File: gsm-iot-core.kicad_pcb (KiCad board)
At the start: 2 copper layers, 38.1 x 61 mm, 95 parts, among them J1 MICRO_SD_HINGE - Micro SD soc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, P1 CONN_01X02, P2 CONN_01X04, P3 CONN_01X15, P4 CONN_01X17, P5 CONN_01X01, P6 CONN_01X01, P7 CONN_01X01, P8 CONN_01X01, P9 Chip anten, Q1 2SC1815, Q2 2SC1815, SW1 SW_PUSH, SW2 SW_PUSH, U1 STM32F405RGTx, U2 MP2365DN, U3 LP2985-50DBVR, U4 MMA7660, U5 SIM800C, U6 SIM HOLD - PPSS-6P, Y1 8MHz, Y2 32.768MHz

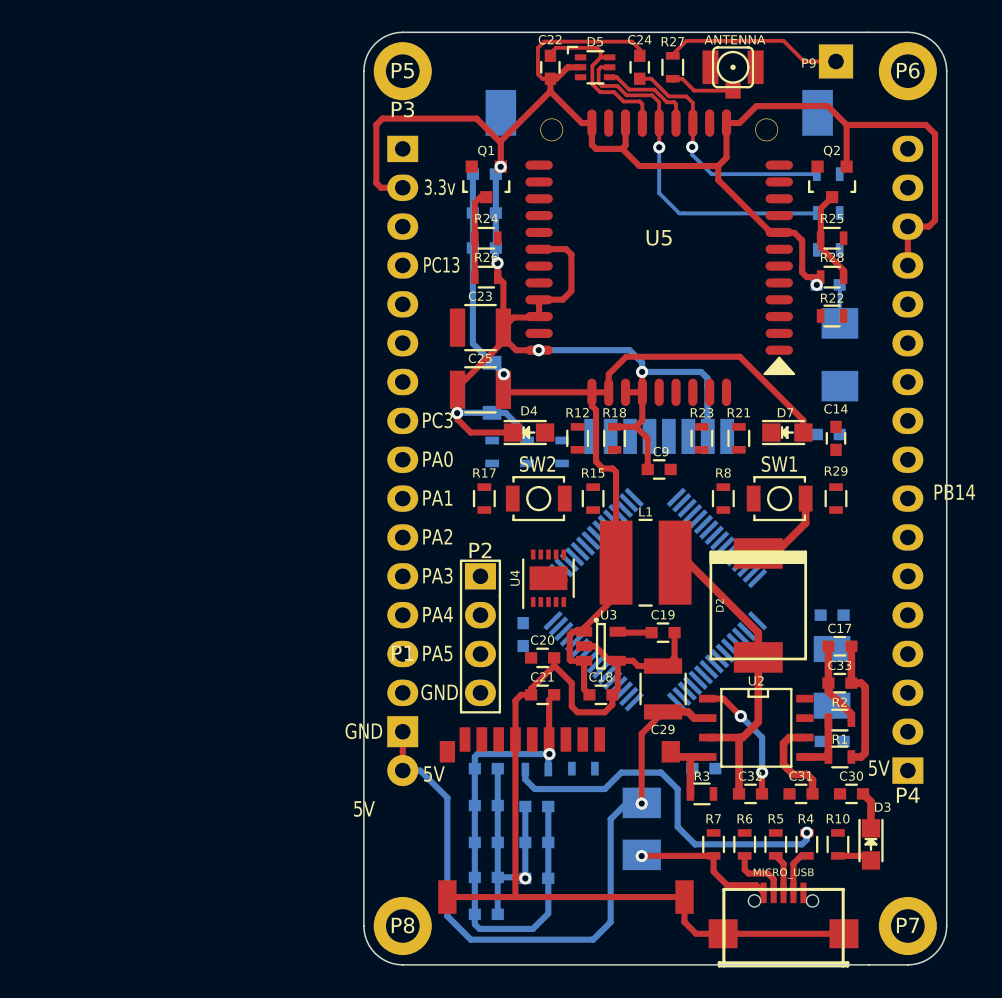
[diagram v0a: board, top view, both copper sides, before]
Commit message: Error add footprint-not updata footprint, local of component is bad
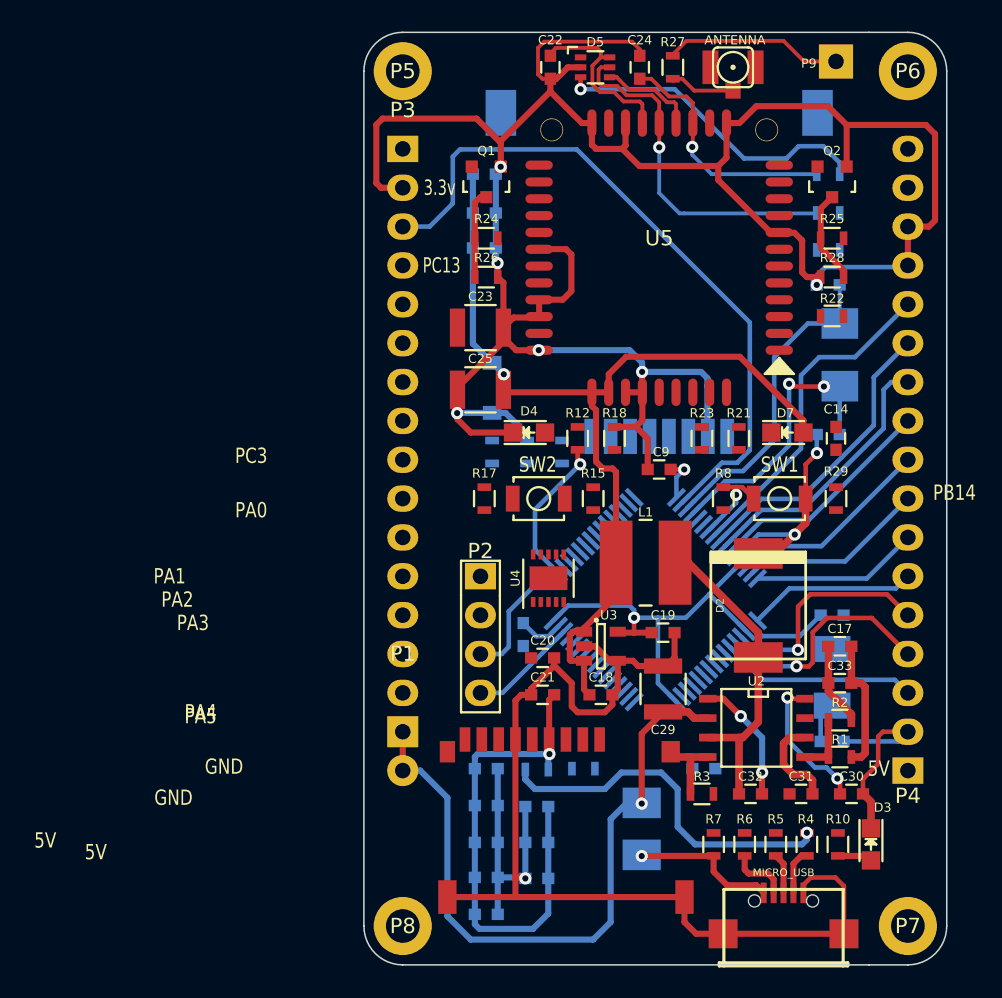
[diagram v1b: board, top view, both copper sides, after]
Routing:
- net PC13: track 0.00 -> 45.5 mm
- net GND: track 257.7 -> 296.4 mm, vias 7 -> 9
- net +3V3: track 35.5 -> 60.8 mm, vias 1 -> 2
- net PC0: track 0.00 -> 21.7 mm
- net Net-(D5-Pad3): track 0.00 -> 21.1 mm, vias 0 -> 1
- net PC1: track 0.00 -> 19.5 mm
- net Net-(C10-Pad1): track 0.00 -> 18.7 mm, vias 0 -> 2
- net Net-(C8-Pad1): track 2.53 -> 20.7 mm
- net PC2: track 0.00 -> 17.9 mm
- net PA5: track 0.00 -> 15.3 mm, vias 0 -> 1
- net PC3: track 0.00 -> 15.1 mm
- net PA4: track 0.00 -> 15.0 mm, vias 0 -> 1
- net PA0: track 0.00 -> 13.5 mm
- net PA6: track 0.00 -> 12.8 mm
- net PA1: track 0.00 -> 12.2 mm
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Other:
- net class Default: trace_width 0.25 -> 0.3
- rule trace_min: 0.25 -> 0.3

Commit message: add assets file and fix README
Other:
- board text removed: "GND"
- board text removed: "PA0"
- board text removed: "PA1"
- board text removed: "PA2"
- board text removed: "PA3"
- board text removed: "PA4"
- board text removed: "PA5"
- board text removed: "PC3"

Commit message: Fix error invalid foortprint- a error footprint file, add new footprint for component
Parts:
- removed ANT1: ANTENNA, w_conn_rf:coaxial_u.fl-r-smt-1
- removed C1, C16, C6: 4.7uF, Capacitors_SMD:C_0603
- removed C10, C8: 15pF, Capacitors_SMD:C_0603
- removed C11: 0.2uF, Capacitors_SMD:C_0603
- removed C12, C13: 27pF, Capacitors_SMD:C_0603
- removed C14, C2, C20, C21, C22, C3, C4, C5, C7, C9: 100nF, Capacitors_SMD:C_0603
- removed C15: 2.2uF, Capacitors_SMD:C_0603
- removed C17, C33: 22uF, Capacitors_SMD:C_0603
- removed C18, C19, C26: 10uF, Capacitors_SMD:C_0603
- removed C23, C25: 100uF, Capacitors_SMD:C_1210
- removed C24: 22pF, Capacitors_SMD:C_0603
- removed C27: 33pF, Capacitors_SMD:C_0603
- removed C28: 10pF, Capacitors_SMD:C_0603
- removed C29: 10uF/35V, Capacitors_SMD:C_1210
- removed C30: 0.1uF, Capacitors_SMD:C_0603
- removed C31: 4.7nF, Capacitors_SMD:C_0603
- removed C32: 10nF, Capacitors_SMD:C_0603
- removed CONN1: MICRO_USB, w_conn_pc:conn_usb_B_micro_smd-2
- removed D1: SS34, Diodes_SMD:DO-214BA
- removed D2: MBRS340, w_smd_diode:do214ab
- removed D3: Led_pwr, LEDs:LED_0805
- removed D4: PA15_LED, LEDs:LED_0805
- removed D5: SMF05C, TO_SOT_Packages_SMD:SC-70-6
- removed D6: zener 5.1v/500mW, Diodes_SMD:SOD-123
- removed D7: Led_SIM, LEDs:LED_0805
- removed J1: MICRO_SD_HINGE - Micro SD socket Push-Push A, lib:MicroSD_Push-Push-A
- removed L1: 6.8uH, Choke_SMD:Choke_SMD_Wuerth-WE-PD2-Typ-MS
- removed P1: CONN_01X02, Pin_Headers:Pin_Header_Straight_1x02
- removed P2: CONN_01X04, Pin_Headers:Pin_Header_Straight_1x04
- removed P3: CONN_01X15, Pin_Headers:Pin_Header_Straight_1x15
- removed P4: CONN_01X17, Pin_Headers:Pin_Header_Straight_1x17
- removed P5, P6, P7, P8: CONN_01X01, Mounting_Holes:MountingHole_2.2mm_M2_DIN965_Pad
- removed P9: Chip anten, Pin_Headers:Pin_Header_Straight_1x01
- removed Q1, Q2: 2SC1815, TO_SOT_Packages_SMD:SOT-23
- removed R1: 25.5k-1%, Resistors_SMD:R_0603
- removed R10, R16, R18, R8: 10k, Resistors_SMD:R_0603
- removed R11: 10M, Resistors_SMD:R_0603
- removed R12: 560R, Resistors_SMD:R_0603
- removed R13, R29, R9: 10K, Resistors_SMD:R_0603
- removed R14: 100k, Resistors_SMD:R_0603
- removed R15, R17, R25, R28: 4.7k, Resistors_SMD:R_0603
- removed R2: 7.5k-1%, Resistors_SMD:R_0603
- removed R21, R22, R23, R7: 1K, Resistors_SMD:R_0603
- removed R24, R26: 4k7, Resistors_SMD:R_0603
- removed R27: 0R, Resistors_SMD:R_0603
- removed R3: 20k, Resistors_SMD:R_0603
- removed R30, R31, R32, R5, R6: 22R, Resistors_SMD:R_0603
- removed R4: DNF-1K, Resistors_SMD:R_0603
- removed SW1, SW2: SW_PUSH, button:SW_SPST_B3U-1000P
- removed U1: STM32F405RGTx, lib:TQFP-64_10x10mm_Pitch0.5mm
- removed U2: MP2365DN, SMD_Packages:SOIC-8-N
- removed U3: LP2985-50DBVR, TO_SOT_Packages_SMD:SOT-23-5
- removed U4: MMA7660, Housings_DFN_QFN:DFN-10-1EP_3x3mm_Pitch0.5mm
- removed U5: SIM800C, lib:SIM800C
- removed U6: SIM HOLD - PPSS-6P, lib:SIM_HOLD_115A-ADA0-R02
- removed Y1: 8MHz, w_crystal:crystal_smd_5x3.2mm
- removed Y2: 32.768MHz, Crystals:Crystal_SMD_5032_2Pads
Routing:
- net GND: track 296.4 -> 0.00 mm, vias 9 -> 0
- net VDD: track 62.3 -> 0.00 mm, vias 1 -> 0
- net +3V3: track 60.8 -> 0.00 mm, vias 2 -> 0
- net PC13: track 45.5 -> 0.00 mm
- net +5V: track 44.6 -> 0.00 mm, vias 2 -> 0
- net PA10_ID: track 23.7 -> 0.00 mm, vias 1 -> 0
- net SIM800C_RST: track 22.9 -> 0.00 mm, vias 1 -> 0
- net PC0: track 21.7 -> 0.00 mm
- net Net-(D5-Pad3): track 21.1 -> 0.00 mm, vias 1 -> 0
- net Net-(C32-Pad1): track 20.8 -> 0.00 mm
- net Net-(C8-Pad1): track 20.7 -> 0.00 mm
- net PC1: track 19.5 -> 0.00 mm
- net Net-(C10-Pad1): track 18.7 -> 0.00 mm, vias 2 -> 0
- net PC2: track 17.9 -> 0.00 mm
- net SIM800C_DATA: track 16.2 -> 0.00 mm, vias 1 -> 0
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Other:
- board outline removed
- board text removed: "3.3v"
- board text removed: "5V"
- board text removed: "PB14"
- board text removed: "PC13"

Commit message: new PCB
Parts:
- added ANT1: ANTENNA, lib:coaxial_u.fl-r-smt-1, F.Cu at (291.8, 67.4)
- added C1: 4.7uF, Capacitors_SMD:C_0603, F.Cu at (151.8, 109.9)
- added C10: 15pF, lib:C_0603, F.Cu at (157.7, 92.6)
- added C11: 0.2uF, lib:C_0603, F.Cu at (157.7, 115.1)
- added C12: 10pF, lib:C_0603, F.Cu at (154.9, 92.7)
- added C13: 10pF, lib:C_0603, F.Cu at (149.1, 98.6)
- added C14: 100nF, lib:C_0603, F.Cu at (148.5, 89.2)
- added C15: 2.2uF, lib:C_0603, F.Cu at (169.2, 108.2)
- added C17: 0.1uF, lib:C_0603, F.Cu at (295.8, 72.1)
- added C18: 100nF, lib:C_0603, F.Cu at (157.7, 96.9)
- added C2: 100nF, Capacitors_SMD:C_0603, F.Cu at (159.9, 116.2)
- added C20: 4.7nF, lib:C_0603, F.Cu at (282.3, 85.2)
- added C21: 10nF, lib:C_0603, F.Cu at (315.1, 52.1)
- added C22: 22uF, lib:C_0603, F.Cu at (319.0, 48.7)
- added C23: 4.7uF, lib:C_0603, F.Cu at (324.3, 45.2)
- added C24: 22uF, lib:C_0603, F.Cu at (276.6, 94.0)
- added C25: 10uF, lib:C_0603, F.Cu at (315.1, 55.5)
- added C26: 10uF, lib:C_0603, F.Cu at (291.1, 76.4)
- added C27: 100nF, lib:C_0603, F.Cu at (291.1, 73.0)
- added C28: 100nF, lib:C_0603, F.Cu at (171.5, 89.2)
- added C29: 10uF/35V, Capacitors_SMD:C_1210, F.Cu at (307.2, 41.5)
- added C3: 100nF, Capacitors_SMD:C_0603, F.Cu at (170.3, 106.0)
- added C34: 100nF, lib:C_0603, F.Cu at (319.0, 52.1)
- added C35: 100nF, lib:C_0603, F.Cu at (165.2, 88.7)
- added C36: 22pF, lib:C_0603, F.Cu at (155.3, 88.7)
- added C37: 100uF, Capacitors_SMD:C_1210, F.Cu at (287.2, 67.7)
- added C38: 100uF, Capacitors_SMD:C_1210, F.Cu at (294.4, 61.1)
- added C39: 10uF, lib:C_0603, F.Cu at (304.7, 66.3)
- added C4: 100nF, Capacitors_SMD:C_0603, F.Cu at (160.3, 96.0)
- added C40: 33pF, lib:C_0603, F.Cu at (267.8, 95.4)
- added C41: 10pF, lib:C_0603, F.Cu at (300.8, 70.4)
- added C5: 100nF, Capacitors_SMD:C_0603, F.Cu at (150.9, 110.7)
- added C6: 4.7uF, Capacitors_SMD:C_0603, F.Cu at (150.0, 111.6)
- added C7: 100nF, Capacitors_SMD:C_0603, F.Cu at (149.1, 112.5)
- added C8: 15pF, lib:C_0603, F.Cu at (164.0, 92.6)
- added CONN1: MICRO_USB, lib:Micro_usb_B_smd, F.Cu at (149.9, 127.0)
- added D1: SS34, lib:do214ac, F.Cu at (114.6, 111.4)
- added D3: MBRS340, lib:do214ab, F.Cu at (287.4, 60.8)
- added D4: Led_pwr, LEDs:LED_0805, F.Cu at (278.5, 80.6)
- added D5: PA15_LED, LEDs:LED_0805, F.Cu at (300.9, 49.6)
- added D6: SMF05C, TO_SOT_Packages_SMD:SC-70-6, F.Cu at (171.5, 85.3)
- added D7: zener 5.1v/500mW, Diodes_SMD:SOD-123, F.Cu at (275.6, 60.4)
- added D8: Led_SIM, LEDs:LED_0805, F.Cu at (300.2, 55.0)
- added J1: MICRO_SD_HINGE - Micro SD socket Push-Push A, MicroSD_Push-Push-A, F.Cu at (171.4, 114.3)
- added L1: 3.3uH-3.2A, Choke_SMD:Choke_SMD_Wuerth-WE-PD2-Typ-MS, F.Cu at (272.8, 69.4)
- added P1: CONN_01X02, Pin_Headers:Pin_Header_Straight_1x02, F.Cu at (182.9, 119.4)
- added P2: CONN_01X04, Pin_Headers:Pin_Header_Straight_1x04, F.Cu at (174.0, 99.1)
- added P3: CONN_01X15, Pin_Headers:Pin_Header_Straight_1x15, F.Cu at (182.9, 78.7)
- added P4: CONN_01X17, Pin_Headers:Pin_Header_Straight_1x17, F.Cu at (137.2, 119.4)
- added P5: Chip anten, lib:point_test, F.Cu at (245.1, 71.1)
- added Q1: 2SC1815, lib:SOT-23, F.Cu at (308.2, 46.9)
- added Q2: 2SC1815, lib:SOT-23, F.Cu at (266.1, 89.0)
- added R10: 20k, lib:R_0603, F.Cu at (284.0, 88.1)
- added R11: 7.5k-1%, lib:R_0603, F.Cu at (263.5, 94.8)
- added R12: 25.5k-1%, lib:R_0603, F.Cu at (270.7, 76.5)
- added R13: 10k, lib:R_0603, F.Cu at (318.5, 54.9)
- added R14: 10M, lib:R_0603, F.Cu at (304.2, 69.1)
- added R15: 560R, lib:R_0603, F.Cu at (298.3, 74.9)
- added R16: 10K, lib:R_0603, F.Cu at (171.5, 87.8)
- added R17: 100k, lib:R_0603, F.Cu at (170.1, 109.1)
- added R18: 4.7k, lib:R_0603, F.Cu at (168.2, 92.6)
- added R19: 10k, lib:R_0603, F.Cu at (171.5, 93.8)
- added R20: 4.7k, lib:R_0603, F.Cu at (166.8, 92.6)
- added R21: 10k, lib:R_0603, F.Cu at (153.3, 114.0)
- added R22: 22R, lib:R_0603, F.Cu at (163.1, 89.7)
- added R23: 22R, lib:R_0603, F.Cu at (160.2, 89.7)
- added R24: 22R, lib:R_0603, F.Cu at (157.3, 89.7)
- added R25: 1K, lib:R_0603, F.Cu at (308.0, 70.1)
- added R26: 1K, lib:R_0603, F.Cu at (299.1, 78.5)
- added R27: 1K, lib:R_0603, F.Cu at (287.8, 89.9)
- added R28: 4k7, lib:R_0603, F.Cu at (295.3, 82.0)
- added R29: 0R, lib:R_0603, F.Cu at (322.2, 55.1)
- added R30: 4.7k, lib:R_0603, F.Cu at (304.2, 72.7)
- added R31: 4k7, lib:R_0603, F.Cu at (316.5, 58.5)
- added R32: 4.7k, lib:R_0603, F.Cu at (287.8, 86.3)
- added R33: 10K, lib:R_0603, F.Cu at (284.0, 91.6)
- added R4: DNF-1K, lib:R_0603, F.Cu at (152.0, 120.7)
- added R5: 22R, lib:R_0603, F.Cu at (150.6, 120.7)
- added R6: 22R, lib:R_0603, F.Cu at (149.1, 120.7)
- added R7: 1K, lib:R_0603, F.Cu at (147.7, 120.7)
- added R8: 10k, lib:R_0603, F.Cu at (148.5, 87.8)
- added R9: 10K, lib:R_0603, F.Cu at (165.4, 92.6)
- added SW1: SW_PUSH, lib:SW_SPST_B3U-1000P-B, F.Cu at (148.5, 91.5)
- added SW3: SW_PUSH, lib:SW_SPST_B3U-1000P-B, F.Cu at (171.5, 91.5)
- added U1: MP2365DN, SMD_Packages:SOIC-8-N, F.Cu at (117.0, 113.2)
- added U2: LP2985-50DBVR, TO_SOT_Packages_SMD:SOT-23-5, F.Cu at (260.6, 83.0)
- added U3: STM32F405RGTx, lib:TQFP-64_10x10mm_Pitch0.5mm, F.Cu at (160.0, 105.9)
- added U4: MMA7660, Housings_DFN_QFN:DFN-10-1EP_3x3mm_Pitch0.5mm, F.Cu at (190.2, 95.5)
- added U5: SIM800C, lib:SIM800C, F.Cu at (160.2, 76.4)
- added U6: SIM HOLD - PPSS-6P, SIM_HOLD_115A-ADA0-R02, B.Cu at (160.0, 87.6)
- added X1: CRYSTAL-24M, lib:Crystal_SMD_5032_4Pads, F.Cu at (152.0, 95.6)
- added Y3: 32.768MHz, lib:crystal_smd_32.768_2Pin, F.Cu at (160.8, 92.6)
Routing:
- net GND: track 0.00 -> 15.3 mm
- net Net-(C8-Pad1): track 0.00 -> 14.1 mm
- net Net-(C12-Pad2): track 0.00 -> 11.6 mm
- net Net-(C10-Pad1): track 0.00 -> 10.7 mm
- net Net-(C13-Pad1): track 0.00 -> 8.79 mm
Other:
- board outline added: 51.2 x 68.6 mm

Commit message: fix 3th
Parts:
- C17, C20, C21, C22, C24, C25, C26, C27, C29, C34, C35, C36, D3, L1, R10, R11, R12, R21, R22, R23, R24, U1, U2, U4: moved to B.Cu
- moved C21 183.1 mm to (148.0, 126.9)
- moved R13 182.8 mm to (148.1, 121.0), turned to 270 degrees
- moved C29 179.4 mm to (148.0, 124.1), turned to 90 degrees
- moved C22 174.6 mm to (162.3, 125.7), turned to 180 degrees
- moved C23 173.8 mm to (158.3, 96.5), turned to 225 degrees
- moved C25 161.9 mm to (168.5, 124.5), turned to 270 degrees
- moved R30 161.5 mm to (142.7, 75.1)
- moved R31 161.3 mm to (155.3, 64.8), turned to 270 degrees
- moved D5 160.5 mm to (157.1, 121.0), turned to 90 degrees
- moved C34 160.0 mm to (172.2, 115.6)
- moved R25 158.7 mm to (149.4, 75.5)
- moved Q1 157.7 mm to (151.5, 64.6), turned to 180 degrees
- moved D3 152.6 mm to (146.3, 118.7), turned to 180 degrees
- moved D8 151.5 mm to (149.0, 64.8), turned to 270 degrees
- moved R26 149.7 mm to (149.4, 76.9)
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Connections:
- P3 pad 10: PB12 -> PC13
- P3 pad 11: PB11 -> PB9
- P3 pad 12: PB10 -> PB8
- P3 pad 13: PB1 -> PB4
- P3 pad 2: GND -> +3V3
- P3 pad 3: PC13 -> GND
- P3 pad 4: PB9 -> PA1
- P3 pad 5: PB8 -> PA0
- P3 pad 6: PB4 -> PC3
- P3 pad 7: PB15 -> PC2
- P3 pad 8: PB14 -> PC1
- P3 pad 9: PB13 -> PC0
- P4 pad 1: +3V3 -> VBAT
- P4 pad 10: PC3 -> PB1
- P4 pad 11: PC2 -> PA6
- P4 pad 12: PC1 -> PA5
- P4 pad 13: PC0 -> PA4
- P4 pad 14: GND -> PA3
- P4 pad 15: GND -> PA2
- P4 pad 16: +3V3 -> GND
- P4 pad 17: VBAT -> +3V3
- P4 pad 2: GND -> +3V3
- P4 pad 3: PA6 -> GND
- P4 pad 4: PA5 -> PB15
- P4 pad 5: PA4 -> PB14
- P4 pad 6: PA3 -> PB13
- P4 pad 7: PA2 -> PB12
- P4 pad 8: PA1 -> PB11
- P4 pad 9: PA0 -> PB10
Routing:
- net GND: track 15.3 -> 81.5 mm, vias 0 -> 1
- net SIM800C_RST: track 0.00 -> 28.3 mm, vias 0 -> 1
- net PA4: track 0.00 -> 23.9 mm
- net PA5: track 0.00 -> 22.2 mm
- net SIM800C_CLK: track 0.00 -> 21.5 mm, vias 0 -> 1
- net PA6: track 0.00 -> 20.9 mm
- net PB15: track 0.00 -> 20.5 mm
- net +3V3: track 0.00 -> 20.5 mm, vias 0 -> 1
- net PB4: track 0.00 -> 19.6 mm, vias 0 -> 1
- net PB1: track 0.00 -> 18.9 mm
- net PB14: track 0.00 -> 18.2 mm
- net PB10: track 0.00 -> 17.4 mm
- net PB13: track 0.00 -> 17.1 mm
- net PC13: track 0.00 -> 17.1 mm, vias 0 -> 1
- net PB9: track 0.00 -> 17.1 mm, vias 0 -> 1
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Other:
- board size 51.2 x 68.6 mm -> 44.7 x 67.6 mm
- net class Default: via_dia 0.8 -> 1.1; via_drill 0.4 -> 0.6

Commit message: PCB new
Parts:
- added D4 (x3): Led_pwr, LEDs:LED_0805, F.Cu at (149.6, 121.0)
- added P8: CONN_01X01, lib:MountingHole_2.5mm, F.Cu at (140.3, 122.6)
- added P8: CONN_01X01, lib:MountingHole_2.5mm, F.Cu at (140.3, 69.2)
- added P8: CONN_01X01, lib:MountingHole_2.5mm, F.Cu at (179.7, 69.2)
- added P8: CONN_01X01, lib:MountingHole_2.5mm, F.Cu at (179.7, 122.6)
- D6: moved to B.Cu
- U3: footprint lib:TQFP-64_10x10mm_Pitch0.5mm -> TQFP-64_10x10mm_Pitch0.5mm
- moved R30 30.5 mm to (172.7, 80.5), turned to 180 degrees
- moved R32 30.0 mm to (172.7, 73.9)
- moved P5 28.6 mm to (148.3, 68.8)
- moved ANT1 23.7 mm to (151.3, 64.4)
- moved R29 23.7 mm to (151.3, 68.0)
- moved Q2 18.0 mm to (172.4, 77.2), turned to 270 degrees
- moved R28 18.0 mm to (148.0, 80.5), turned to 0 degrees
- moved R27 17.2 mm to (158.6, 88.6), turned to 90 degrees
- moved R25 16.9 mm to (160.0, 88.6), turned to 90 degrees
- moved R26 16.8 mm to (161.4, 88.6), turned to 90 degrees
- moved C37 15.0 mm to (160.0, 64.4)
- moved L1 14.5 mm to (146.7, 118.7), turned to 270 degrees
- moved C34 13.9 mm to (166.1, 128.2)
- moved Q1 13.0 mm to (147.6, 77.1), turned to 90 degrees
- moved R31 11.7 mm to (148.0, 73.9), turned to 0 degrees
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- renumbered SW1 to RST
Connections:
- P1 pad 2: +5V -> VBAT
- P4 pad 1: VBAT -> +3V3
- P4 pad 2: +3V3 -> GND
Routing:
- net GND: track 81.5 -> 409.3 mm, vias 1 -> 17
- net +3V3: track 20.5 -> 252.0 mm, vias 1 -> 15
- net VDD: track 11.0 -> 117.7 mm, vias 0 -> 5
- net SIM800C_DATA: track 9.05 -> 65.4 mm, vias 1 -> 4
- net /PB2: track 0.00 -> 54.5 mm, vias 0 -> 5
- net PA7_PWRKEY: track 0.00 -> 45.6 mm, vias 0 -> 4
- net +5V: track 5.75 -> 42.2 mm, vias 1 -> 2
- net SIM800C_TXD: track 0.00 -> 33.5 mm, vias 0 -> 2
- net PB3_BUTTON: track 0.00 -> 32.2 mm, vias 0 -> 2
- net PA2: track 0.00 -> 31.5 mm, vias 0 -> 3
- net SIM800C_RXD: track 0.00 -> 31.5 mm, vias 0 -> 2
- net PA3: track 0.00 -> 29.3 mm, vias 0 -> 3
- net /PB5: track 6.93 -> 36.1 mm, vias 0 -> 1
- net /RST: track 0.00 -> 27.7 mm, vias 0 -> 2
- net PC3: track 0.00 -> 26.8 mm, vias 0 -> 1
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- added copper zone on B.Cu, net GND
- added copper zone on F.Cu, net GND
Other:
- board text added: "3.3V"
- board text added: "5V"
- board text added: "GND"
- board text added: "PA0"
- board text added: "PA1"
- board text added: "PA2"
- board text added: "PA3"
- board text added: "PA4"
- board text added: "PA5"
- board text added: "PA6"
- board text added: "PB1"
- board text added: "PB10"
- board text added: "PB11"
- board text added: "PB12"
- board text added: "PB13"
- board text added: "PB14"
- board text added: "PB15"
- board text added: "PC0"
- board text added: "PC1"
- board text added: "PC13"
- board text added: "PC2"
- board text added: "PC3"
- board text added: "PC4"
- board text added: "PC8"
- board text added: "PC9"
- board text added: "SWCLK"
- board text added: "SWDIO"
- board text added: "VBAT"
